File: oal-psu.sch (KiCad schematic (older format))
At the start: 35 parts, among them P1 120V-MAINS, P1A REGA_VOLTAGE, P1B REGB_VOLTAGE, P2 OUTPUT, P3 OUTPUT_SELECT, P4A CONTROL_A, P4B CONTROL_B, T1 TRANSFO_DUAL-DUAL, U1A TPS7A4700, U1B TPS7A4700

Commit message: cap bank
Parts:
- removed D1A, D1B: Diode_Bridge, symbol Diode_Bridge
- removed P1A: REGA_VOLTAGE, symbol CONN_02X08
- removed P1B: REGB_VOLTAGE, symbol CONN_02X08
- added C1A1, C1A3, C1A4, C1A5, C1B1, C1B3, C1B4, C1B5: 1kuF, symbol CP
- added D1A, D1B, D2A, D2B, D3A (x2), D4A (x2): DIODE-45, symbol DIODE-45
- added SW1A: VOLTAGE_A, symbol 8DIP_SWITCH
- added SW1B: VOLTAGE_B, symbol 8DIP_SWITCH
- C1A2, C1B2: renamed from C1A; value 5k8uF -> 1kuF
- T1: value TRANSFO_DUAL-DUAL -> TALEMA 15/25VA
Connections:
- net labels removed: NEG-A, NEG-B
- wire segments 120 -> 128
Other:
- note added: "+"
- note added: "-"
- note added: "AC"
- note added: "~"
- moved on the sheet: 10uF, C1A2, C1B2, C5A, C6A, C7A, C8A, C9A, D2A, D2B, F1, P1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

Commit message: finalizing schematic
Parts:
- removed F1: FUSE, symbol FUSE
- removed P4A: CONTROL_A, symbol CONN_01X04
- removed P4B: CONTROL_B, symbol CONN_01X04
- added CsA, CsB: 0.1uF, symbol C
- added CxA, CxB: 0.01uF, symbol C
- added J1: 120V-LINE, symbol CONN_01X02
- added J4A: UNREG_A, symbol CONN_01X03
- added J4B: UNREG_B, symbol CONN_01X03
- added P2A: ENABLE_A, symbol CONN_01X02
- added P2B: ENABLE_B, symbol CONN_01X02
- added RsA, RsB: R, symbol R
- J2: renamed from P1; value 120V-MAINS -> 120V-NEUTRAL
- R1A, R1B: value XRX -> 820R
- renumbered P2 to J3, D2A to LED1A, D2B to LED1B, P3 to P1
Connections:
- net labels added: NEG-A, NEG-B
- wire segments 128 -> 240
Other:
- note added: "1-2 - LOCAL SENSE A\n3-4 - BIPOLAR\n5-6 - LOCAL SENSE B"
- moved on the sheet: J2, J3, T1

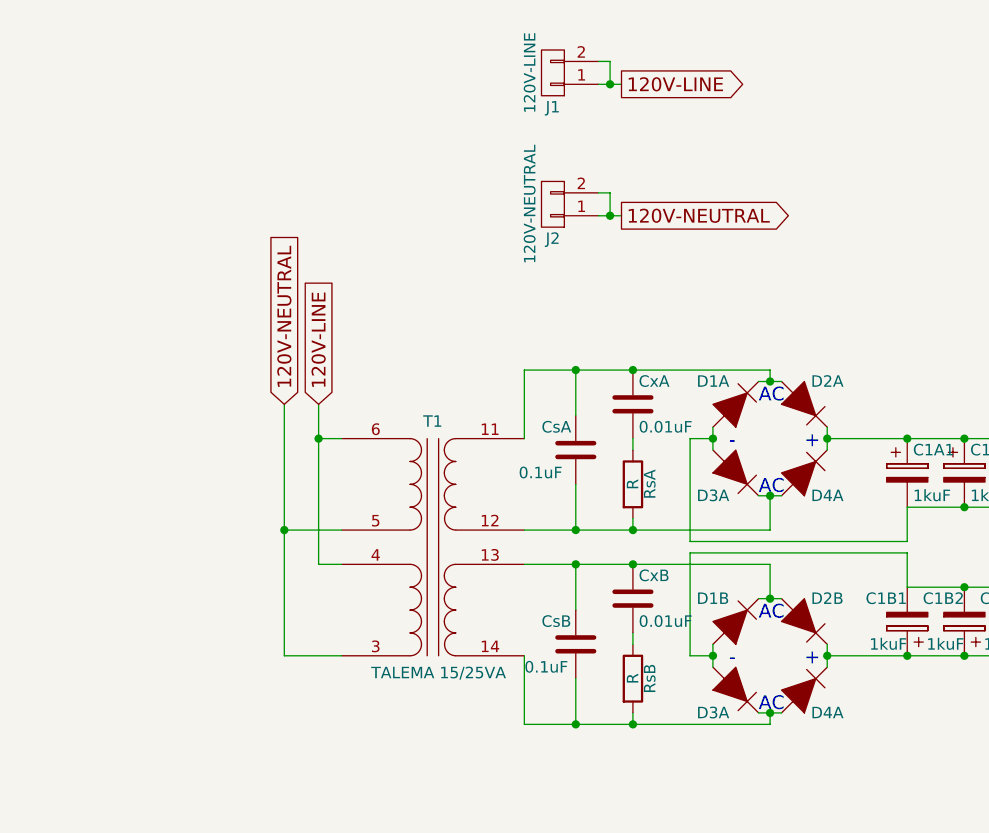
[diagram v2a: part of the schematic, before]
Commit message: mains voltage select switch
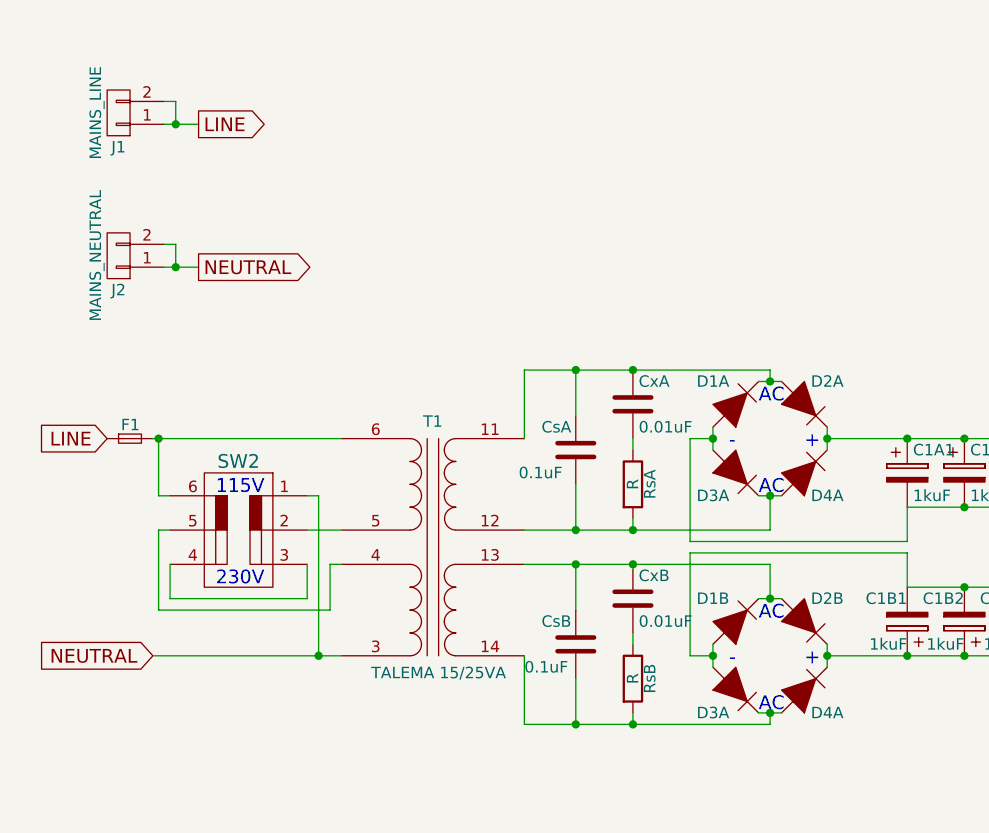
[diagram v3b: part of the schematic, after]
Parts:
- added F1: F_Small, symbol F_Small
- added SW2: DPDT_SLIDE, symbol DPDT_SLIDE
- J1: value 120V-LINE -> MAINS_LINE
- J2: value 120V-NEUTRAL -> MAINS_NEUTRAL
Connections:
- net 120V-LINE renamed LINE
- net LINE: now also F1.1; no longer T1.4 (PRIMARY2-DOT), T1.6 (PRIMARY1-DOT)
- net 120V-NEUTRAL renamed NEUTRAL
- net NEUTRAL: now also SW2.1; no longer T1.5 (PRIMARY1-NODOT)
- new net: SW2.5, T1.4 (PRIMARY2-DOT)
- new net: SW2.2, T1.5 (PRIMARY1-NODOT)
- new net: F1.2, SW2.6, T1.6 (PRIMARY1-DOT)
- new net: SW2.3, SW2.4
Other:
- note added: "115V"
- note added: "230V"
- moved on the sheet: J1, J2
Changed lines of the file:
@@
 Text GLabel 8950 4000 2    60   Output ~ 0
 POS-B
-Text GLabel 1675 2600 1    60   Input ~ 0
-120V-LINE
-Text GLabel 1525 2600 1    60   Input ~ 0
-120V-NEUTRAL
+Text GLabel 750  2750 0    60   Input ~ 0
+LINE
+Text GLabel 950  3700 0    60   Input ~ 0
+NEUTRAL
 Text GLabel 8150 1000 2    60   Output ~ 0
 GND-A
@@
 L CONN_01X02 J2
 U 1 1 56C3204B
-P 2700 1725
-F 0 "J2" H 2700 1875 50  0000 C CNN
-F 1 "120V-NEUTRAL" V 2800 1725 50  0000 C CNN
-F 2 "" H 2700 1725 50  0000 C CNN
-F 3 "" H 2700 1725 50  0000 C CNN
-	1    2700 1725
+P 800 1950
+F 0 "J2" H 800 2100 50  0000 C CNN
+F 1 "MAINS_NEUTRAL" V 900 1950 50  0000 C CNN
+F 2 "" H 800 1950 50  0000 C CNN
+F 3 "" H 800 1950 50  0000 C CNN
+	1    800  1950
 	-1   0    0    1
 $EndComp
-Text GLabel 3000 1775 2    60   Output ~ 0
-120V-NEUTRAL
+Text GLabel 1150 2000 2    60   Output ~ 0
+NEUTRAL
 Text GLabel 9875 1175 2    60   Input ~ 0
 POS-A
@@
 Text Notes 3650 2450 0    60   ~ 0
 ~
-Text Notes 3500 950  0    60   ~ 0
+Text Notes 1600 1125 0    60   ~ 0
 ~
 Text Notes 3600 2600 0    60   ~ 0
@@
 L CONN_01X02 J1
 U 1 1 56CFDE2E
-P 2700 1150
-F 0 "J1" H 2700 1300 50  0000 C CNN
-F 1 "120V-LINE" V 2800 1150 50  0000 C CNN
-F 2 "" H 2700 1150 50  0000 C CNN
-F 3 "" H 2700 1150 50  0000 C CNN
-	1    2700 1150
+P 800 1325
+F 0 "J1" H 800 1475 50  0000 C CNN
+F 1 "MAINS_LINE" V 900 1325 50  0000 C CNN
+F 2 "" H 800 1325 50  0000 C CNN
+F 3 "" H 800 1325 50  0000 C CNN
+	1    800  1325
 	-1   0    0    1
 $EndComp
-Text GLabel 3000 1200 2    60   Output ~ 0
-120V-LINE
+Text GLabel 1150 1375 2    60   Output ~ 0
+LINE
+$Comp
+L DPDT_SLIDE SW2
+U 1 1 56D137C5
+P 1325 3150
+F 0 "SW2" V 1025 3150 60  0000 C CNN
+F 1 "DPDT_SLIDE" V 1625 3150 60  0001 C CNN
+F 2 "" H 1325 3150 60  0000 C CNN
+F 3 "" H 1325 3150 60  0000 C CNN
+	1    1325 3150
+	0    1    1    0
+$EndComp
+Text Notes 1225 3000 0    60   ~ 0
+115V
+Text Notes 1225 3400 0    60   ~ 0
+230V
 Connection ~ 5650 2450
 Wire Wire Line
@@
 Wire Wire Line
 	5100 1850 5100 2075
-Wire Wire Line
-	1675 2750 1775 2750
 Connection ~ 3400 3700
 Wire Wire Line
@@
 	7750 4300 8950 4300
 Wire Wire Line
+	7750 2350 7750 2450
+Wire Wire Line
 	7750 2450 7750 2500
 Connection ~ 5750 3400
@@
 	9825 1175 9875 1175
 Wire Wire Line
-	2900 1775 2950 1775
-Wire Wire Line
-	2950 1775 3000 1775
+	1000 2000 1050 2000
+Wire Wire Line
+	1050 2000 1150 2000
 Connection ~ 7750 2850
 Wire Wire Line
@@
 Wire Wire Line
 	5750 4000 5750 4100
-Connection ~ 1525 3150
-Wire Wire Line
-	1525 3700 1775 3700
-Connection ~ 1675 2750
-Wire Wire Line
-	1675 3300 1775 3300
-Wire Wire Line
-	1675 2600 1675 2750
-Wire Wire Line
-	1675 2750 1675 3300
-Wire Wire Line
-	1525 3150 1775 3150
 Wire Wire Line
 	6400 1000 6500 1000
@@
 Connection ~ 5650 4000
 Wire Wire Line
-	1525 2600 1525 3150
-Wire Wire Line
-	1525 3150 1525 3700
-Wire Wire Line
-	2900 1675 2950 1675
-Wire Wire Line
-	2950 1675 2950 1775
-Connection ~ 2950 1775
-Wire Wire Line
-	2900 1200 2950 1200
-Wire Wire Line
-	2950 1200 3000 1200
-Wire Wire Line
-	2950 1100 2950 1200
-Connection ~ 2950 1200
-Wire Wire Line
-	2950 1100 2900 1100
+	1000 1900 1050 1900
+Wire Wire Line
+	1050 1900 1050 2000
+Connection ~ 1050 2000
+Wire Wire Line
+	1000 1375 1050 1375
+Wire Wire Line
+	1050 1375 1150 1375
+Wire Wire Line
+	1050 1275 1050 1375
+Connection ~ 1050 1375
+Wire Wire Line
+	1050 1275 1000 1275
 Connection ~ 7750 2350
-Wire Wire Line
-	7750 2350 7750 2450
 Wire Wire Line
 	7750 2350 8050 2350
 Connection ~ 5750 2050
 Connection ~ 5750 4400
+Wire Wire Line
+	950  2750 975  2750
+Wire Wire Line
+	975  2750 1775 2750
+Wire Wire Line
+	950  3700 1675 3700
+Wire Wire Line
+	1675 3700 1775 3700
+Wire Wire Line
+	1625 3150 1775 3150
+Wire Wire Line
+	1725 3300 1775 3300
+Wire Wire Line
+	1625 3000 1675 3000
+Wire Wire Line
+	1675 3000 1675 3700
+Connection ~ 1675 3700
+Wire Wire Line
+	975  3000 1025 3000
+Wire Wire Line
+	975  3000 975  2750
+Connection ~ 975  2750
+Wire Wire Line
+	1025 3150 975  3150
+Wire Wire Line
+	975  3150 975  3500
+Wire Wire Line
+	975  3500 1725 3500
+Wire Wire Line
+	1725 3500 1725 3300
+$Comp
+L F_Small F1
+U 1 1 56D1B0FF
+P 850 2750
+F 0 "F1" H 810 2810 50  0000 L CNN
+F 1 "F_Small" H 730 2690 50  0001 L CNN
+F 2 "" H 850 2750 50  0000 C CNN
+F 3 "" H 850 2750 50  0000 C CNN
+	1    850  2750
+	1    0    0    -1
+$EndComp
+Wire Wire Line
+	1025 3300 1025 3450
+Wire Wire Line
+	1025 3450 1625 3450
+Wire Wire Line
+	1625 3450 1625 3300
 $EndSCHEMATC

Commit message: finializing initial circuit pass
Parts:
- removed F1: F_Small, symbol F_Small
- removed J3: OUTPUT, symbol CONN_01X06
- removed J4A: UNREG_A, symbol CONN_01X03
- removed J4B: UNREG_B, symbol CONN_01X03
- removed P2B: ENABLE_B, symbol CONN_01X02
- added F1: FUSE, symbol FUSE
- added J1: OUTPUT, symbol CONN_01X12
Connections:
- net LINE: now also F1.1
- net NEG-A: now also P1.3 (P3), J1.11 (P11), J1.7 (P7); no longer P1.5 (P5)
- net NEG-B: now also J1.2 (P2), J1.5 (P5)
- net POS-A: now also J1.8 (P8)
- net POS-B: now also P1.4 (P4), P1.5 (P5), J1.6 (P6); no longer P1.3 (P3), P1.6 (P6)
- net SENSE-A: now also J1.9 (P9)
- net SENSE-B: now also P1.6 (P6), J1.4 (P4); no longer P1.4 (P4)
- net UNREG-A: now reaches C1A1.1, C1A2.1, C1A3.1, C1A4.1, C1A5.1, C2A.1, C3A.1, D2A.2 (CATHODE), D4A.2 (CATHODE), P2A.1 (P1), U1A.15 (IN), U1A.16 (IN)
- net UNREG-A: now also J1.12 (P12)
- net UNREG-B: now reaches 10uF.2, C1B1.1, C1B2.1, C1B3.1, C1B4.1, C1B5.1, C2B.1, D2B.2 (CATHODE), D4A.2 (CATHODE), U1B.15 (IN), U1B.16 (IN)
- net UNREG-B: now also J1.1 (P1)
- net ENABLE-A: now reaches P2A.2 (P2), U1A.13 (EN)
- net ENABLE-A: now also J1.10 (P10)
- net at SW2.6, T1.6 (PRIMARY1-DOT): now also F1.2
- net ENABLE-B: now reaches U1B.13 (EN)
- net ENABLE-B: now also J1.3 (P3)
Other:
- moved on the sheet: 10uF, C1A1, C1A2, C1A3, C1A4, C1A5, C1B1, C1B2, C1B3, C1B4, C1B5, C2A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

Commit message: initial layout work
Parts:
- added P201: ENABLE_B, Pin_Headers:Pin_Header_Straight_1x02, symbol CONN_01X02
- C101: renamed from CsA; footprint (none) -> ose-audio-labs:TDK-B32529-63VAC
- C102: renamed from CxA; footprint (none) -> ose-audio-labs:TDK-B32529-63VAC
- C103: renamed from C1A1; footprint (none) -> ose-audio-labs:35V-LYTIC-7.5-5
- C104: renamed from C1A2; footprint (none) -> ose-audio-labs:35V-LYTIC-7.5-5
- C105: renamed from C1A3; footprint (none) -> ose-audio-labs:35V-LYTIC-7.5-5-10snap
- C106: renamed from C1A4; footprint (none) -> ose-audio-labs:35V-LYTIC-7.5-5
- C107: renamed from C1A5; footprint (none) -> ose-audio-labs:35V-LYTIC-7.5-5
- C108: renamed from C2A; footprint (none) -> Capacitors_Tantalum_SMD:TantalC_SizeD_EIA-7343_Reflow
- C109: renamed from C3A; footprint (none) -> Capacitors_SMD:C_1206
- C110: renamed from C4A; footprint (none) -> Capacitors_SMD:C_0805
- C111: renamed from C5A; footprint (none) -> Capacitors_SMD:C_1206
- C112: renamed from C6A; footprint (none) -> Capacitors_SMD:C_1206
- C113: renamed from C7A; footprint (none) -> Capacitors_SMD:C_1206
- C114: renamed from C8A; footprint (none) -> Capacitors_SMD:C_1206
- C115: renamed from C9A; footprint (none) -> Capacitors_SMD:C_1206
- C201: renamed from CsB; footprint (none) -> ose-audio-labs:TDK-B32529-63VAC
- C202: renamed from CxB; footprint (none) -> ose-audio-labs:TDK-B32529-63VAC
- C203: renamed from C1B1; footprint (none) -> ose-audio-labs:35V-LYTIC-7.5-5
- C204: renamed from C1B2; footprint (none) -> ose-audio-labs:35V-LYTIC-7.5-5
- C205: renamed from C1B3; footprint (none) -> ose-audio-labs:35V-LYTIC-7.5-5
- C206: renamed from C1B4; footprint (none) -> ose-audio-labs:35V-LYTIC-7.5-5
- C207: renamed from C1B5; footprint (none) -> ose-audio-labs:35V-LYTIC-7.5-5-10snap
- C208: renamed from C2B; footprint (none) -> Capacitors_Tantalum_SMD:TantalC_SizeD_EIA-7343_Reflow
- C209: renamed from 10uF; value C3B -> 10uF; footprint (none) -> Capacitors_SMD:C_1206
- C210: renamed from C4B; footprint (none) -> Capacitors_SMD:C_0805
- C211: renamed from 10uF; value C5B -> 10uF; footprint (none) -> Capacitors_SMD:C_1206
- C212: renamed from 10uF; value C6B -> 10uF; footprint (none) -> Capacitors_SMD:C_1206
- C213: renamed from 10uF; value C7B -> 10uF; footprint (none) -> Capacitors_SMD:C_1206
- C214: renamed from 10uF; value C8B -> 10uF; footprint (none) -> Capacitors_SMD:C_1206
- C215: renamed from 10uF; value C9B -> 10uF; footprint (none) -> Capacitors_SMD:C_1206
- D101: renamed from D1A; footprint (none) -> ose-audio-labs:DO-221AC
- D102: renamed from D2A; footprint (none) -> ose-audio-labs:DO-221AC
- D103, D203: renamed from D3A; footprint (none) -> ose-audio-labs:DO-221AC
- D104, D204: renamed from D4A; footprint (none) -> ose-audio-labs:DO-221AC
- D201: renamed from D1B; footprint (none) -> ose-audio-labs:DO-221AC
- D202: renamed from D2B; footprint (none) -> ose-audio-labs:DO-221AC
- F1: footprint (none) -> ose-audio-labs:LITTLEFUSE-0PTF0078P
- J1, J2: footprint (none) -> ose-audio-labs:PHEONIX_SPT_5-2POS
- J3: renamed from J1; footprint (none) -> ose-audio-labs:PHEONIX_MC1.5-12-G-3.5
- LED101: renamed from LED1A; footprint (none) -> LEDs:LED-1206
- LED201: renamed from LED1B; footprint (none) -> LEDs:LED-1206
- P101: renamed from P2A; footprint (none) -> Pin_Headers:Pin_Header_Straight_1x02
- P2: renamed from P1; footprint (none) -> Pin_Headers:Pin_Header_Straight_2x03
- R101: renamed from RsA; footprint (none) -> Resistors_SMD:R_1210
- R102: renamed from R1A; footprint (none) -> Resistors_SMD:R_0805
- R201: renamed from RsB; footprint (none) -> Resistors_SMD:R_1210
- R202: renamed from R1B; footprint (none) -> Resistors_SMD:R_0805
- SW1: renamed from SW2; footprint (none) -> ose-audio-labs:CK_V80212MS02Q-VOLTAGE_SELECTOR
- SW102: renamed from SW1A; footprint (none) -> ose-audio-labs:DIP8-HALF-PITCH
- SW202: renamed from SW1B; footprint (none) -> ose-audio-labs:DIP8-HALF-PITCH
- T1: footprint (none) -> ose-audio-labs:TALEMA_70000K_35VA
- U101: renamed from U1A; footprint (none) -> ose-audio-labs:PVQFN-N20
- U201: renamed from U1B; footprint (none) -> ose-audio-labs:PVQFN-N20
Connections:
- net GND-A is gone; now on net NEG-A: C110.1, R102.1, SW102.10 (7B), SW102.11 (6B), SW102.12 (5B), SW102.13 (4B), SW102.14 (3B), SW102.15 (2B), SW102.16 (1B), SW102.9 (8B)
- net GND-B is gone; now on net NEG-B: C210.1, R202.1, SW202.10 (7B), SW202.11 (6B), SW202.12 (5B), SW202.13 (4B), SW202.14 (3B), SW202.15 (2B), SW202.16 (1B), SW202.9 (8B)
- net ENABLE-B: now also P201.2 (P2)
- net NEG-B: now also C209.2, C211.1, C212.1, C213.1, C214.1, C215.1; no longer C209.1, C211.2, C212.2, C213.2, C214.2, C215.2
- net POS-B: now also C211.2, C212.2, C213.2, C214.2, C215.2; no longer C211.1, C212.1, C213.1, C214.1, C215.1
- net UNREG-B: now also C209.1, P201.1 (P1); no longer C209.2
- net at U101.10 (0P4V): now also SW102.3 (3A); no longer SW102.6 (6A)
- net at U101.11 (0P2V): now also SW102.2 (2A); no longer SW102.7 (7A)
- net at U101.12 (0P1V): now also SW102.1 (1A); no longer SW102.8 (8A)
- net at U101.4 (6P4V2): now also SW102.8 (8A); no longer SW102.1 (1A)
- net at U101.5 (6P4V1): now also SW102.7 (7A); no longer SW102.2 (2A)
- net at U101.6 (3P2V): now also SW102.6 (6A); no longer SW102.3 (3A)
- net at U101.8 (1P6V): now also SW102.5 (5A); no longer SW102.4 (4A)
- net at U101.9 (0P8V): now also SW102.4 (4A); no longer SW102.5 (5A)
